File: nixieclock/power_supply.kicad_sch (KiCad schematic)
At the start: 38 parts, among them J1 USB_C_Receptacle, Q1 IRLR3110ZTRPBF, Q2 AO3401A, U1 LT3757AEMSE, U3 LMR64010XMF, U4 AMS1117-3.3

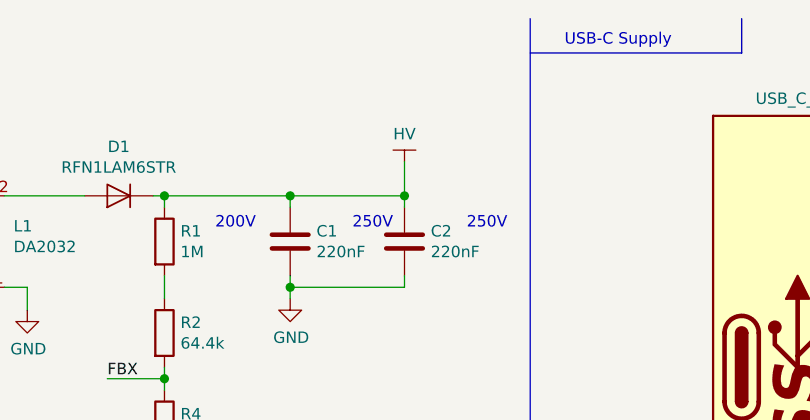
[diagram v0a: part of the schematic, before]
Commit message: added neon bulbs, finalized cathode registers
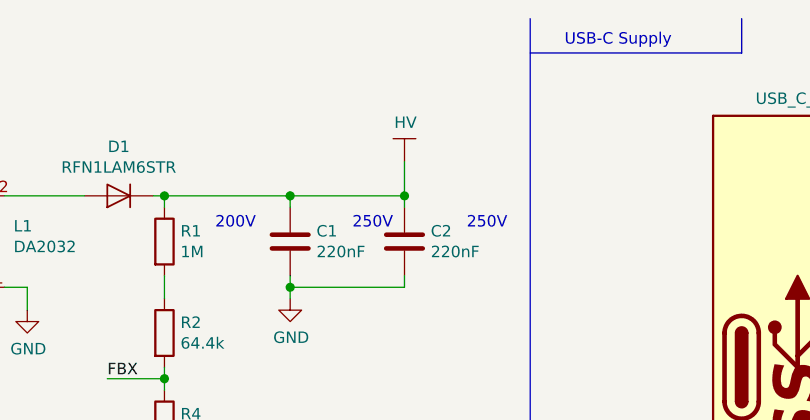
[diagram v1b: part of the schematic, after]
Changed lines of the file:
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@@
   (title_block
     (title "Nixie Clock - Power Supply")
-    (date "2021-03-14")
+    (date "2021-03-15")
     (company "Bastian de Byl")
     (comment 1 "https://github.com/tonyp7/170v-nixie-power-supply/")
@@
   (junction (at 224.79 25.4) (diameter 1.016) (color 0 0 0 0))
   (junction (at 264.16 25.4) (diameter 1.016) (color 0 0 0 0))
+  (no_connect (at 200.66 91.44))
+  (no_connect (at 223.52 83.82))
+  (no_connect (at 223.52 68.58))
+  (no_connect (at 223.52 60.96))
+  (no_connect (at 223.52 45.72))
+  (no_connect (at 223.52 76.2))
+  (no_connect (at 223.52 58.42))
+  (no_connect (at 223.52 40.64))
+  (no_connect (at 223.52 53.34))
+  (no_connect (at 223.52 30.48))
+  (no_connect (at 223.52 66.04))
+  (no_connect (at 223.52 50.8))
+  (no_connect (at 223.52 43.18))
+  (no_connect (at 223.52 38.1))
+  (no_connect (at 223.52 81.28))
   (no_connect (at 223.52 73.66))
   (no_connect (at 223.52 33.02))
-  (no_connect (at 223.52 53.34))
-  (no_connect (at 223.52 83.82))
-  (no_connect (at 223.52 45.72))
-  (no_connect (at 223.52 81.28))
-  (no_connect (at 200.66 91.44))
-  (no_connect (at 223.52 68.58))
-  (no_connect (at 223.52 76.2))
-  (no_connect (at 223.52 66.04))
-  (no_connect (at 223.52 40.64))
-  (no_connect (at 223.52 50.8))
-  (no_connect (at 223.52 43.18))
-  (no_connect (at 223.52 60.96))
-  (no_connect (at 223.52 58.42))
-  (no_connect (at 223.52 30.48))
-  (no_connect (at 223.52 38.1))
   (wire (pts (xy 25.4 24.13) (xy 25.4 25.4))
     (stroke (width 0) (type solid) (color 0 0 0 0))
@@
   (global_label "~SHDN" (shape input) (at 41.91 58.42 180)
     (effects (font (size 1.27 1.27)) (justify right))
-  )
-  (symbol (lib_id "Personal:HV") (at 163.83 27.94 0) (unit 1)
-    (in_bom no) (on_board no)
-    (property "Reference" "#PWR02" (id 0) (at 163.83 29.21 0)
-      (effects (font (size 1.27 1.27)) hide)
-    )
-    (property "Value" "HV" (id 1) (at 163.83 24.8852 0))
-    (property "Footprint" "" (id 2) (at 163.83 27.94 0)
-      (effects (font (size 1.27 1.27)) hide)
-    )
-    (property "Datasheet" "" (id 3) (at 163.83 27.94 0)
-      (effects (font (size 1.27 1.27)) hide)
-    )
   )
   (symbol (lib_id "power:VCC") (at 25.4 24.13 0) (unit 1)
@@
       (effects (font (size 1.27 1.27)) hide)
     )
+  )
+  (symbol (lib_id "Personal:HV") (at 163.83 27.94 0) (unit 1)
+    (in_bom yes) (on_board yes)
+    (property "Reference" "#PWR0104" (id 0) (at 163.83 31.75 0)
+      (effects (font (size 1.27 1.27)) hide)
+    )
+    (property "Value" "HV" (id 1) (at 163.9441 23.6152 0))
+    (property "Footprint" "" (id 2) (at 163.83 27.94 0)
+      (effects (font (size 1.27 1.27)) hide)
+    )
+    (property "Datasheet" "" (id 3) (at 163.83 27.94 0)
+      (effects (font (size 1.27 1.27)) hide)
+    )

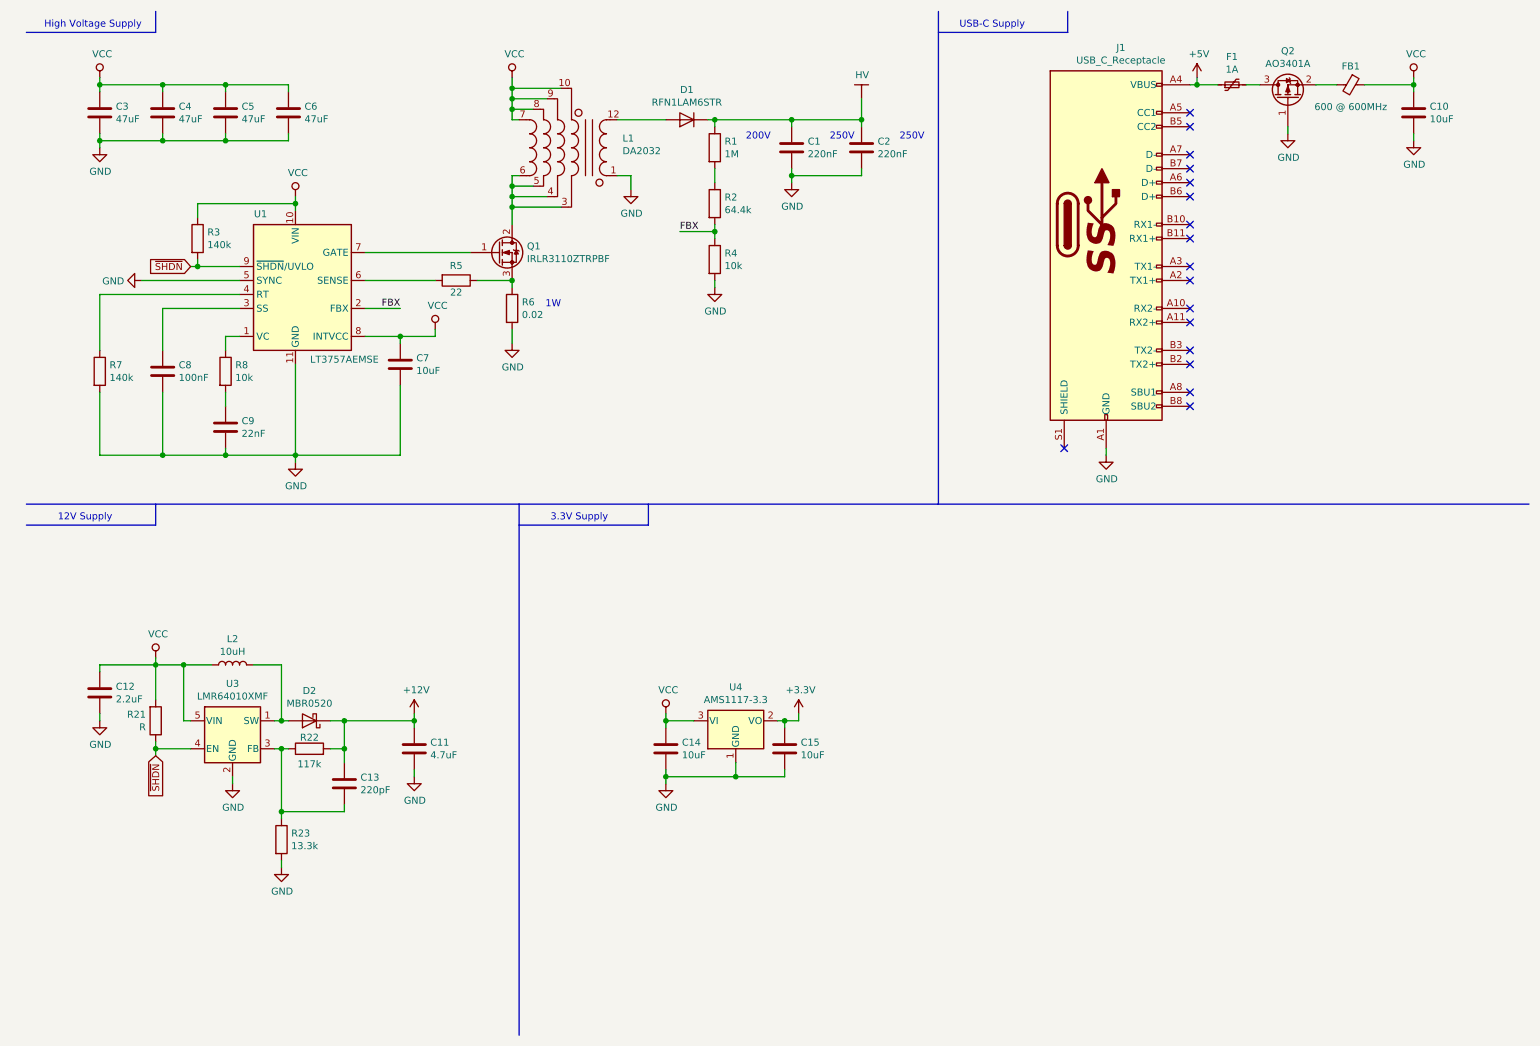
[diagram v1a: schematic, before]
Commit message: began routing PCB, finalized registers design
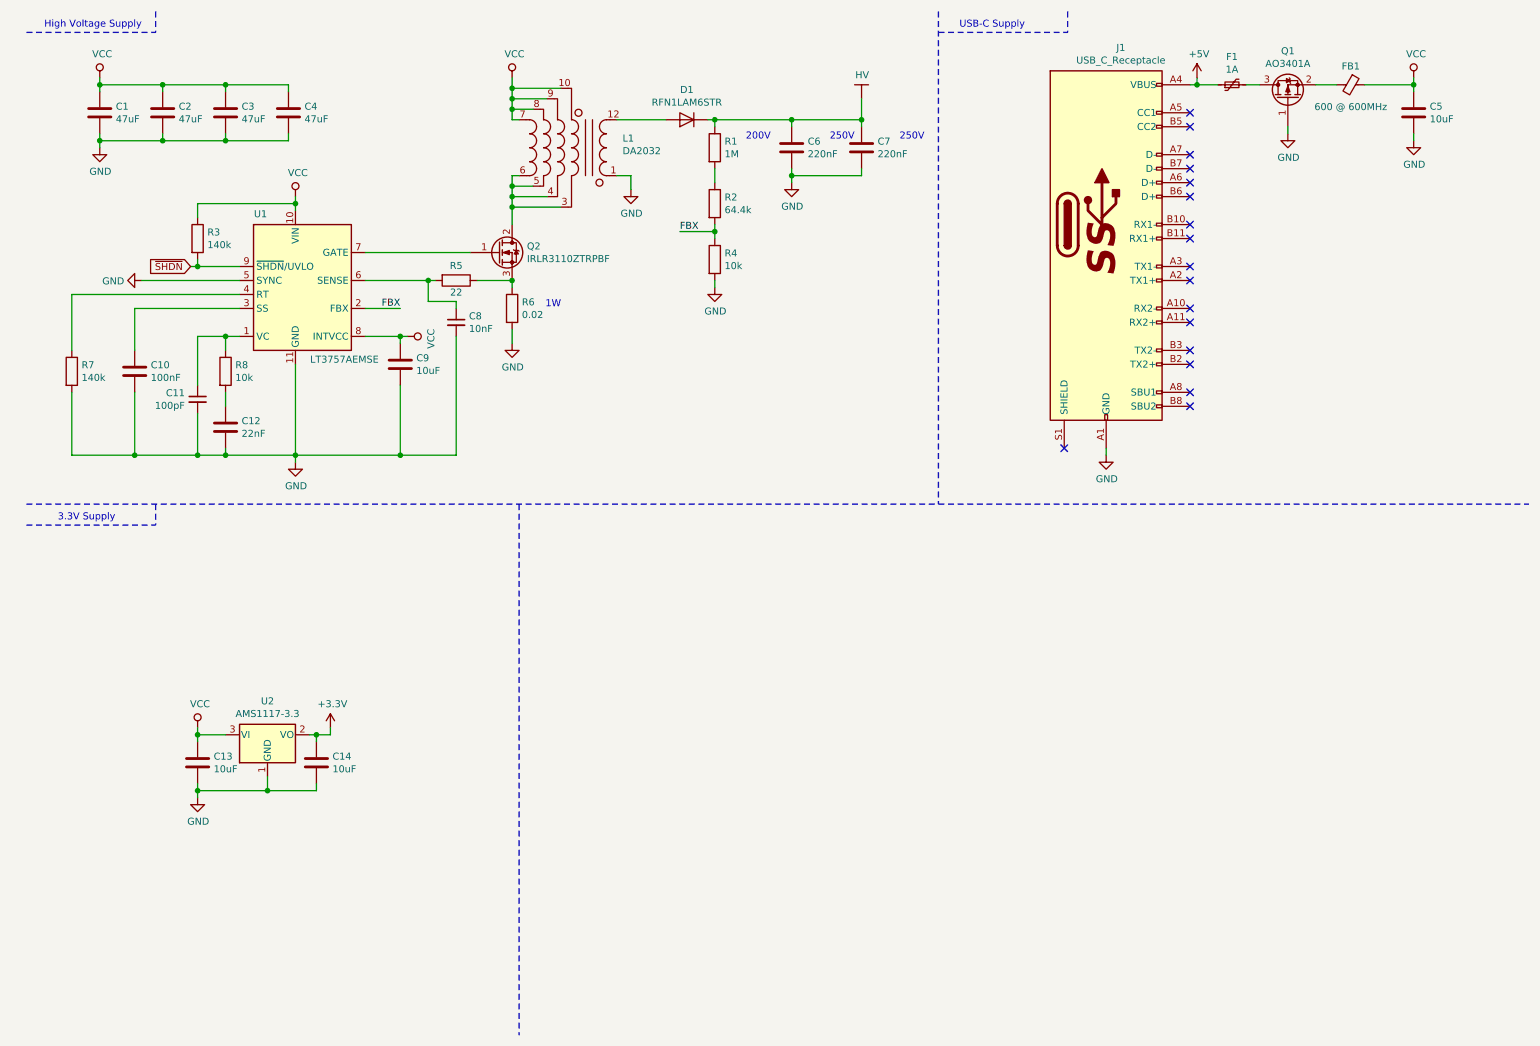
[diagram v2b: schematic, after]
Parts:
- removed C11: 4.7uF, Capacitor_SMD:C_1206_3216Metric_Pad1.42x1.75mm_HandSolder, symbol Device:C
- removed C12: 2.2uF, Capacitor_SMD:C_0805_2012Metric_Pad1.15x1.40mm_HandSolder, symbol Device:C
- removed C13: 220pF, Capacitor_SMD:C_0805_2012Metric_Pad1.15x1.40mm_HandSolder, symbol Device:C
- removed D2: MBR0520, Diode_SMD:D_SOD-123, symbol Diode:MBR0520
- removed L2: 10uH, Personal:MSS1048-103MLB, symbol Device:L
- removed R21: R, Resistor_SMD:R_0805_2012Metric_Pad1.15x1.40mm_HandSolder, symbol Device:R
- removed R22: 117k, Resistor_SMD:R_0805_2012Metric_Pad1.15x1.40mm_HandSolder, symbol Device:R
- removed R23: 13.3k, Resistor_SMD:R_0805_2012Metric_Pad1.15x1.40mm_HandSolder, symbol Device:R
- removed U3: LMR64010XMF, Package_TO_SOT_SMD:SOT-23-5, symbol Regulator_Switching:LMR64010XMF
- added C11: 100pF, Capacitor_SMD:C_0603_1608Metric_Pad1.05x0.95mm_HandSolder, symbol Device:C_Small
- added C8: 10nF, Capacitor_SMD:C_0603_1608Metric_Pad1.05x0.95mm_HandSolder, symbol Device:C_Small
- R6: footprint Resistor_SMD:R_0603_1608Metric_Pad1.05x0.95mm_HandSolder -> Resistor_SMD:R_1206_3216Metric_Pad1.42x1.75mm_HandSolder
- renumbered C3 to C1, C8 to C10, C9 to C12, C14 to C13, C15 to C14, C4 to C2, C5 to C3, C6 to C4, C10 to C5, C1 to C6, C2 to C7, C7 to C9, Q2 to Q1, Q1 to Q2, U4 to U2
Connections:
- net GND: now also C11.2, C8.2
- net at R8.1, U1.1 (VC): now also C11.1
- net at R5.2, U1.6 (SENSE): now also C8.1
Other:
- note removed: "12V Supply"
- company: Bastian de Byl -> (none)
- moved on the sheet: C10, C13, C14, R7, U2

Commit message: mostly finalized pcb layout, silkscreen graphics, etc
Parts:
- J1: footprint (none) -> Connector_USB:USB_C_Receptacle_Amphenol_12401610E4-2A
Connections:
- net +3V3: now also R3.1
- net VCC: no longer R3.1
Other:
- company: (none) -> Bastian de Byl
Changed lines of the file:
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@@
   (title_block
     (title "Nixie Clock - Power Supply")
-    (date "2021-03-18")
+    (date "2021-03-19")
+    (company "Bastian de Byl")
     (comment 1 "https://github.com/tonyp7/170v-nixie-power-supply/")
     (comment 2 "Original HV source from 'tonyp7'")
@@
   (junction (at 48.26 92.71) (diameter 1.016) (color 0 0 0 0))
   (junction (at 55.88 153.67) (diameter 1.016) (color 0 0 0 0))
-  (junction (at 60.96 46.99) (diameter 1.016) (color 0 0 0 0))
   (junction (at 60.96 92.71) (diameter 1.016) (color 0 0 0 0))
   (junction (at 64.77 143.51) (diameter 1.016) (color 0 0 0 0))
@@
     (stroke (width 0) (type solid) (color 0 0 0 0))
   )
-  (wire (pts (xy 43.18 46.99) (xy 60.96 46.99))
-    (stroke (width 0) (type solid) (color 0 0 0 0))
-  )
-  (wire (pts (xy 43.18 49.53) (xy 43.18 46.99))
+  (wire (pts (xy 43.18 48.26) (xy 43.18 49.53))
     (stroke (width 0) (type solid) (color 0 0 0 0))
   )
@@
     (stroke (width 0) (type solid) (color 0 0 0 0))
   )
-  (wire (pts (xy 43.18 142.24) (xy 43.18 143.51))
+  (wire (pts (xy 43.18 138.43) (xy 43.18 143.51))
     (stroke (width 0) (type solid) (color 0 0 0 0))
   )
@@
     (stroke (width 0) (type solid) (color 0 0 0 0))
   )
-  (wire (pts (xy 60.96 45.72) (xy 60.96 46.99))
-    (stroke (width 0) (type solid) (color 0 0 0 0))
-  )
-  (wire (pts (xy 60.96 46.99) (xy 60.96 48.26))
+  (wire (pts (xy 60.96 45.72) (xy 60.96 48.26))
     (stroke (width 0) (type solid) (color 0 0 0 0))
   )
@@
     (stroke (width 0) (type solid) (color 0 0 0 0))
   )
+  (wire (pts (xy 64.77 138.43) (xy 64.77 143.51))
+    (stroke (width 0) (type solid) (color 0 0 0 0))
+  )
   (wire (pts (xy 64.77 143.51) (xy 64.77 144.78))
     (stroke (width 0) (type solid) (color 0 0 0 0))
   )
-  (wire (pts (xy 64.77 143.51) (xy 67.31 143.51))
-    (stroke (width 0) (type solid) (color 0 0 0 0))
-  )
   (wire (pts (xy 64.77 152.4) (xy 64.77 153.67))
-    (stroke (width 0) (type solid) (color 0 0 0 0))
-  )
-  (wire (pts (xy 67.31 142.24) (xy 67.31 143.51))
     (stroke (width 0) (type solid) (color 0 0 0 0))
   )
@@
     (effects (font (size 1.27 1.27)) (justify left bottom))
   )
-  (global_label "~SHDN" (shape input) (at 41.91 58.42 180)
+  (hierarchical_label "~SHDN" (shape input) (at 41.91 58.42 180)
     (effects (font (size 1.27 1.27)) (justify right))
-    (property "Intersheet References" "${INTERSHEET_REFS}" (id 0) (at 0 0 0)
-      (effects (font (size 1.27 1.27)) hide)
-    )
   )
   (symbol (lib_id "power:VCC") (at 25.4 24.13 0) (unit 1)
@@
     (pin "1")
   )
-  (symbol (lib_id "power:VCC") (at 43.18 142.24 0) (unit 1)
-    (in_bom yes) (on_board yes)
-    (property "Reference" "#PWR018" (id 0) (at 43.18 146.05 0)
-      (effects (font (size 1.27 1.27)) hide)
-    )
-    (property "Value" "VCC" (id 1) (at 43.6118 137.9156 0))
-    (property "Footprint" "" (id 2) (at 43.18 142.24 0)
-      (effects (font (size 1.27 1.27)) hide)
-    )
-    (property "Datasheet" "" (id 3) (at 43.18 142.24 0)
+  (symbol (lib_id "power:VCC") (at 43.18 138.43 0) (unit 1)
+    (in_bom yes) (on_board yes)
+    (property "Reference" "#PWR018" (id 0) (at 43.18 142.24 0)
+      (effects (font (size 1.27 1.27)) hide)
+    )
+    (property "Value" "VCC" (id 1) (at 43.6118 134.1056 0))
+    (property "Footprint" "" (id 2) (at 43.18 138.43 0)
+      (effects (font (size 1.27 1.27)) hide)
+    )
+    (property "Datasheet" "" (id 3) (at 43.18 138.43 0)
       (effects (font (size 1.27 1.27)) hide)
     )
@@
     (pin "1")
   )
-  (symbol (lib_id "power:+3.3V") (at 67.31 142.24 0) (unit 1)
-    (in_bom yes) (on_board yes)
-    (property "Reference" "#PWR019" (id 0) (at 67.31 146.05 0)
-      (effects (font (size 1.27 1.27)) hide)
-    )
-    (property "Value" "+3.3V" (id 1) (at 67.6783 137.9156 0))
-    (property "Footprint" "" (id 2) (at 67.31 142.24 0)
-      (effects (font (size 1.27 1.27)) hide)
-    )
-    (property "Datasheet" "" (id 3) (at 67.31 142.24 0)
+  (symbol (lib_id "power:+3.3V") (at 43.18 48.26 0) (unit 1)
+    (in_bom yes) (on_board yes)
+    (property "Reference" "#PWR080" (id 0) (at 43.18 52.07 0)
+      (effects (font (size 1.27 1.27)) hide)
+    )
+    (property "Value" "+3.3V" (id 1) (at 43.18 44.7126 0))
+    (property "Footprint" "" (id 2) (at 43.18 48.26 0)
+      (effects (font (size 1.27 1.27)) hide)
+    )
+    (property "Datasheet" "" (id 3) (at 43.18 48.26 0)
+      (effects (font (size 1.27 1.27)) hide)
+    )
+    (pin "1")
+  )
+  (symbol (lib_id "power:+3.3V") (at 64.77 138.43 0) (unit 1)
+    (in_bom yes) (on_board yes)
+    (property "Reference" "#PWR019" (id 0) (at 64.77 142.24 0)
+      (effects (font (size 1.27 1.27)) hide)
+    )
+    (property "Value" "+3.3V" (id 1) (at 65.1383 134.1056 0))
+    (property "Footprint" "" (id 2) (at 64.77 138.43 0)
+      (effects (font (size 1.27 1.27)) hide)
+    )
+    (property "Datasheet" "" (id 3) (at 64.77 138.43 0)
       (effects (font (size 1.27 1.27)) hide)
     )
@@
     (property "Reference" "J1" (id 0) (at 210.947 18.6498 0))
     (property "Value" "USB_C_Receptacle" (id 1) (at 210.947 20.9485 0))
-    (property "Footprint" "" (id 2) (at 212.09 50.8 0)
-      (effects (font (size 1.27 1.27)) hide)
-    )
+    (property "Footprint" "Connector_USB:USB_C_Receptacle_Amphenol_12401610E4-2A" (id 2) (at 212.09 50.8 0)
+      (effects (font (size 1.27 1.27)) hide)
+    )
